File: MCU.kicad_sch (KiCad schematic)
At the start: 44 parts, among them J12 duPont, SW11 SW_QSPI, SW12 SW_RUN, U11 W25Q128JVS, U12 RP2350_60QFN, Y11 ABM8_262_T3

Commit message: v1.0.1 - RF Fix
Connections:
- net RF_IRQ: now reaches U12.36 (GPIO24)
- no-connect marks 10 -> 9
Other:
- note added: "Need to add IRQ into a gpio pin"
- note added: "PROBABLY NEED TO BREAKOUT MORE PINS JUST IN CASE"
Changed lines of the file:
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@@
 	(title_block
 		(title "Microcontroller RP2350A")
-		(date "2025-07-01")
-		(rev "A")
+		(date "2026-02-27")
+		(rev "1.0.1")
 		(company "Bronco STAR - BLV")
 	)
@@
 		)
 	)
+	(text "PROBABLY NEED TO BREAKOUT MORE PINS JUST IN CASE\n"
+		(exclude_from_sim no)
+		(at 283.21 199.39 0)
+		(effects
+			(font
+				(size 1.27 1.27)
+			)
+		)
+	)
+	(text "Need to add IRQ into a gpio pin"
+		(exclude_from_sim no)
+		(at 268.478 184.658 0)
+		(effects
+			(font
+				(size 1.27 1.27)
+			)
+		)
+	)
 	(text "1V1 Integrated VReg @ max 200mA\n\n"
 		(exclude_from_sim no)
@@
 	)
 	(no_connect
-		(at 243.84 177.8)
-	)
-	(no_connect
 		(at 243.84 134.62)
 	)
@@
 	(wire
 		(pts
-			(xy 243.84 172.72) (xy 247.65 172.72)
+			(xy 243.84 172.72) (xy 264.16 172.72)
 		)
 		(stroke
@@
 	(wire
 		(pts
-			(xy 243.84 170.18) (xy 247.65 170.18)
+			(xy 243.84 170.18) (xy 264.16 170.18)
 		)
 		(stroke
@@
 	(wire
 		(pts
+			(xy 243.84 177.8) (xy 264.16 177.8)
+		)
+		(stroke
+			(width 0)
+			(type default)
+		)
+	)
+	(wire
+		(pts
 			(xy 180.34 143.51) (xy 176.53 143.51)
 		)
@@
 	(wire
 		(pts
-			(xy 243.84 175.26) (xy 247.65 175.26)
+			(xy 243.84 175.26) (xy 264.16 175.26)
 		)
 		(stroke
@@
 	(hierarchical_label "RF_TXEN"
 		(shape input)
-		(at 247.65 175.26 0)
+		(at 264.16 175.26 0)
 		(effects
 			(font
@@
 	(hierarchical_label "RF_RXEN"
 		(shape input)
-		(at 247.65 172.72 0)
+		(at 264.16 172.72 0)
 		(effects
 			(font
@@
 	(hierarchical_label "RF_RST"
 		(shape output)
-		(at 247.65 170.18 0)
+		(at 264.16 170.18 0)
 		(effects
 			(font
@@
 		(effects
 			(font
+				(size 1.27 1.27)
+			)
+			(justify left)
+		)
+	)
+	(hierarchical_label "RF_IRQ"
+		(shape output)
+		(at 264.16 177.8 0)
+		(effects
+			(font

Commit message: v1.0.1
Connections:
- net RF_IRQ: now also U12.34 (GPIO22); no longer U12.36 (GPIO24)
- net RF_RXEN: now also U12.35 (GPIO23); no longer U12.34 (GPIO22)
- net RF_TXEN: now also U12.36 (GPIO24); no longer U12.35 (GPIO23)
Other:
- note added: "1V1 Integrated VReg @ 200mA"
- note added: "PROBABLY NEED TO BREAKOUT MORE PINS JUST IN CASE BREAK OUT SPI"
- note added: "RF_IRQ - for v0.1 Software,use one of the UART2 pin"
- note removed: "1V1 Integrated VReg @ max 200mA"
- note removed: "Need to add IRQ into a gpio pin"
- note removed: "PROBABLY NEED TO BREAKOUT MORE PINS JUST IN CASE"
- moved on the sheet: C11, C12, C18, R14, R16, Y11

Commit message: init v1.0.2
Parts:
- R26, R27, R28: value 470 -> 1k
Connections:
- net SPI1_CS2 is gone; now on net SPI1_CS1: U12.17 (GPIO13)
- net +3V3: no longer SW12.2, U12.26 (RUN)
- net SPI1_CS1: no longer U12.15 (GPIO11)
- new net: SW12.2, U12.26 (RUN)
- new net SPI1_CS0: U12.15 (GPIO11)
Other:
- note added: "CS0 = SD_CARD CS1 = GNSS"
- note removed: "RF_IRQ - for v0.1 Software,use one of the UART2 pin"
- moved on the sheet: D11, D12, D13, J12, R26, R27, R28

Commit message: v1.0.2 changelog
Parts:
- D11, D12, D13: value GREEN -> KT-0805G
- SW11: value SW_QSPI -> SW_Push; footprint Button_Switch_SMD:SW_SPST_B3U-1000P -> Button_Switch_SMD:SW_Push_1P1T_NO_CK_KMR2
- SW12: value SW_RUN -> SW_Push; footprint Button_Switch_SMD:SW_SPST_B3U-1000P -> Button_Switch_SMD:SW_Push_1P1T_NO_CK_KMR2
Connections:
- net RUN: now reaches SW12.2, U12.26 (RUN)
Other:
- note added: "Add TVS on UART2"
- moved on the sheet: D11, D12, D13, R26, R27, R28

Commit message: safepoint
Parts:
- J12: value duPont -> PinHeader_01x03_Pin
- SW11, SW12: value SW_Push -> KMR2
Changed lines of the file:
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@@
 			)
 		)
-		(property "Value" "duPont"
+		(property "Value" "PinHeader_01x03_Pin"
 			(at 149.86 182.8799 0)
 			(effects
@@
 			)
 		)
-		(property "Value" "SW_Push"
+		(property "Value" "KMR2"
 			(at 160.02 165.1 0)
 			(effects
@@
 			)
 		)
-		(property "Value" "SW_Push"
+		(property "Value" "KMR2"
 			(at 146.05 137.1599 90)
 			(effects

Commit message: Post-manufacturing v1 check.
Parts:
- C13, C16, C19, C20, C21, C22, C23, C24, C25, C26: LCSC Part C1525 -> (none)
- C17, C18: LCSC Part C23733 -> (none)
- SW11, SW12: LCSC Part C720477 -> (none)
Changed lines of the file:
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@@
 			)
 		)
-		(property "LCSC Part" "C1525"
+		(property "LCSC Part" ""
 			(at 236.22 64.77 0)
 			(effects
@@
 			)
 		)
-		(property "LCSC Part" "C1525"
+		(property "LCSC Part" ""
 			(at 311.15 64.77 0)
 			(effects
@@
 			)
 		)
-		(property "LCSC Part" "C1525"
+		(property "LCSC Part" ""
 			(at 153.67 64.77 0)
 			(effects
@@
 			)
 		)
-		(property "LCSC Part" "C1525"
+		(property "LCSC Part" ""
 			(at 299.72 64.77 0)
 			(effects
@@
 			)
 		)
-		(property "LCSC Part" "C1525"
+		(property "LCSC Part" ""
 			(at 72.39 115.57 0)
 			(effects
@@
 			)
 		)
-		(property "LCSC Part" "C23733"
+		(property "LCSC Part" ""
 			(at 166.37 101.6 0)
 			(effects
@@
 			)
 		)
-		(property "LCSC Part" "C1525"
+		(property "LCSC Part" ""
 			(at 179.07 64.77 0)
 			(effects
@@
 			)
 		)
-		(property "LCSC Part" "C720477"
+		(property "LCSC Part" ""
 			(at 160.02 170.18 0)
 			(effects
@@
 			)
 		)
-		(property "LCSC Part" "C1525"
+		(property "LCSC Part" ""
 			(at 287.02 64.77 0)
 			(effects
@@
 			)
 		)
-		(property "LCSC Part" "C1525"
+		(property "LCSC Part" ""
 			(at 248.92 64.77 0)
 			(effects
@@
 			)
 		)
-		(property "LCSC Part" "C720477"
+		(property "LCSC Part" ""
 			(at 144.78 135.89 90)
 			(effects
@@
 			)
 		)
-		(property "LCSC Part" "C23733"
+		(property "LCSC Part" ""
 			(at 166.37 64.77 0)
 			(effects
@@
 			)
 		)
-		(property "LCSC Part" "C1525"
+		(property "LCSC Part" ""
 			(at 274.32 64.77 0)
 			(effects
@@
 			)
 		)
-		(property "LCSC Part" "C1525"
+		(property "LCSC Part" ""
 			(at 261.62 64.77 0)
 			(effects

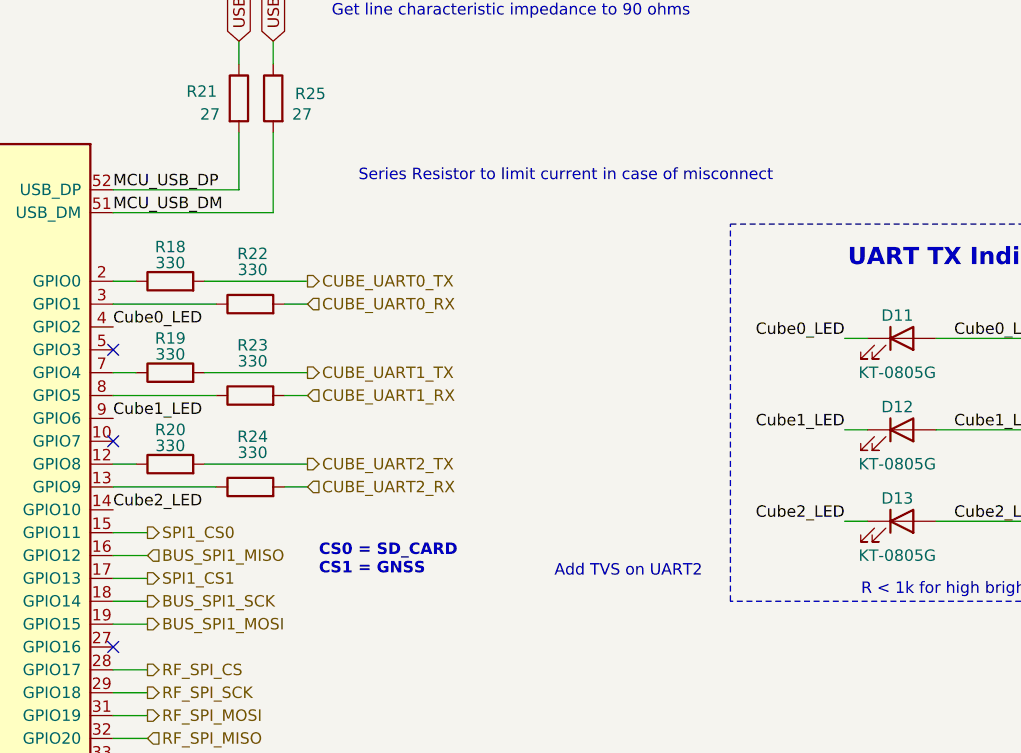
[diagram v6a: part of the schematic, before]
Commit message: Breakout SPI1 buses & rename CS
- Add SPI bus 1 CS pin names
- Breakout SPI bus 1
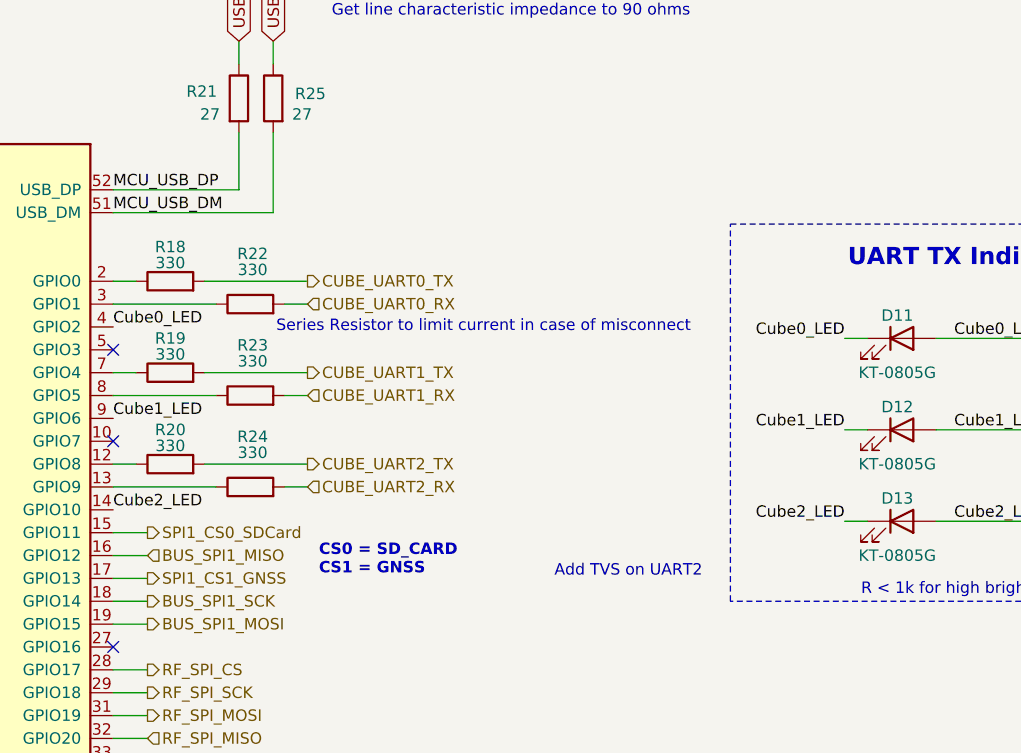
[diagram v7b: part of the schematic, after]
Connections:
- net SPI1_CS0 renamed SPI1_CS0_SDCard
- net SPI1_CS1 renamed SPI1_CS1_GNSS
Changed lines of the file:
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@@
 	(text "Series Resistor to limit current in case of misconnect\n"
 		(exclude_from_sim no)
-		(at 294.132 105.156 0)
+		(at 284.988 121.92 0)
 		(effects
 			(font
@@
 		)
 	)
-	(hierarchical_label "SPI1_CS1"
+	(hierarchical_label "SPI1_CS1_GNSS"
 		(shape output)
 		(at 247.65 149.86 0)
@@
 		)
 	)
-	(hierarchical_label "SPI1_CS0"
+	(hierarchical_label "SPI1_CS0_SDCard"
 		(shape output)
 		(at 247.65 144.78 0)
